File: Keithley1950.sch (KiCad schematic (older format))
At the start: 81 parts, among them J1 Conn_01x14, J2 Conn_01x03, J3 Conn_01x02, K1 Relay_SP2P, K2 Relay_SP2P, K3 Relay_SP3P, K4 Relay_SP2P, K5 Relay_SP2P, K6 Relay_SP3P, K7 Relay_SP3P, Q1 MMBFJ111, Q2 MMBFJ111, Q3 MMBFJ111, Q4 MMBFJ111, Q5 MMBT3906, Q6 MMBT3906, Q7 MMBFJ111, Q8 MMBT3906, U1 TL082, U2 LM339, U3 74LS138, U4 AD8436, U5 ULN2003, U6 74HC4094, U7 TL082

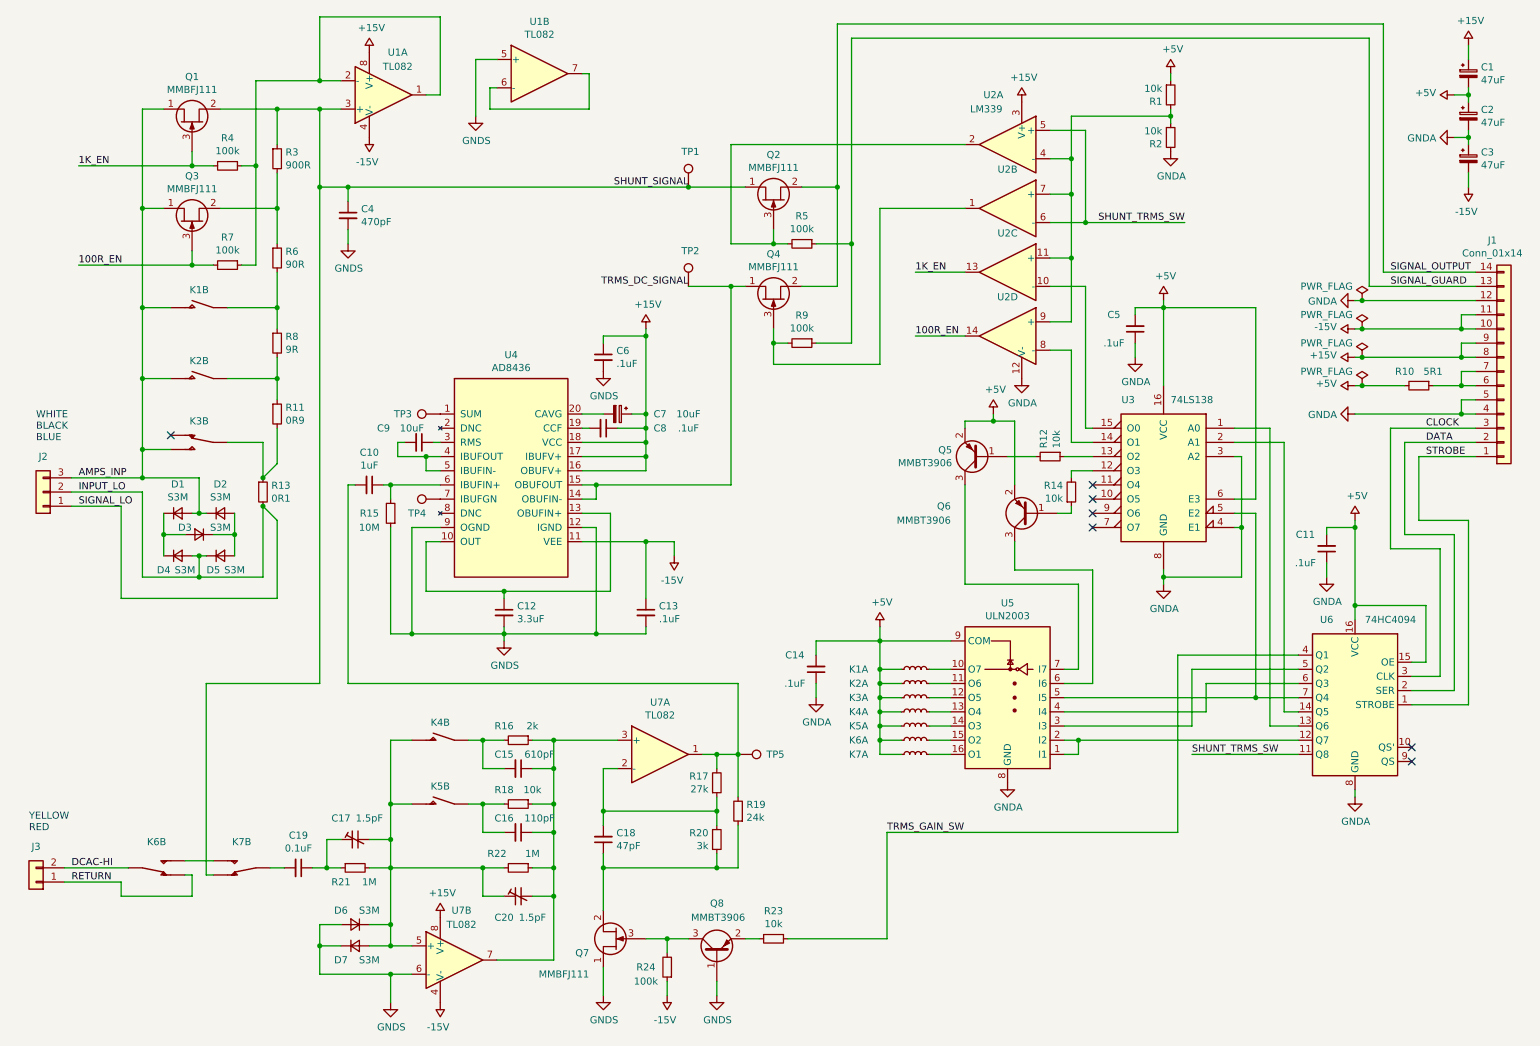
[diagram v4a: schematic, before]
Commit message: Switch to 2 serial resistors for shunts in schematic
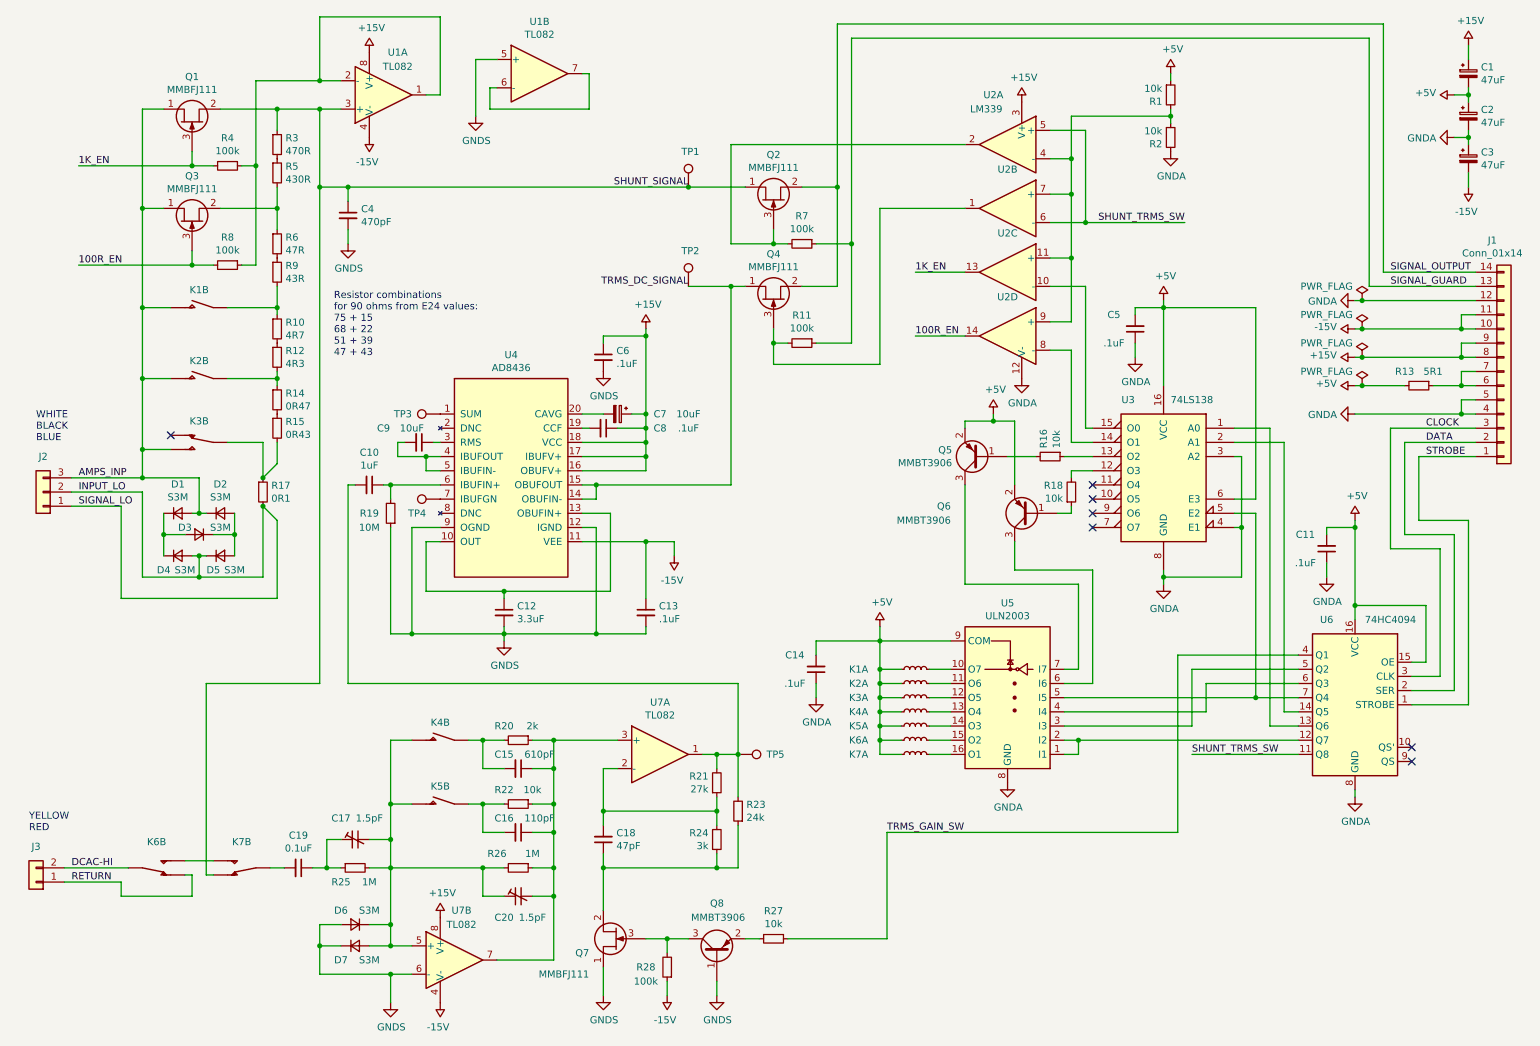
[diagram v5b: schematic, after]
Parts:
- added R10: 4R7, Resistor_SMD:R_0805_2012Metric, symbol Device:R_Small
- added R14: 0R47, Resistor_SMD:R_2512_6332Metric, symbol Device:R_Small
- added R3: 470R, Resistor_SMD:R_0805_2012Metric, symbol Device:R_Small
- added R6: 47R, Resistor_SMD:R_0805_2012Metric, symbol Device:R_Small
- R12: renamed from R8; value 9R -> 4R3
- R15: renamed from R11; value 0R9 -> 0R43; footprint project:R_2512_x2_serial -> Resistor_SMD:R_2512_6332Metric
- R5: renamed from R3; value 900R -> 430R; footprint project:R_0805_x2_Serial -> Resistor_SMD:R_0805_2012Metric
- R9: renamed from R6; value 90R -> 43R; footprint project:R_0805_x2_Serial -> Resistor_SMD:R_0805_2012Metric
- renumbered R9 to R11, R10 to R13, R12 to R16, R13 to R17, R14 to R18, R15 to R19, R16 to R20, R17 to R21, R18 to R22, R19 to R23, R20 to R24, R21 to R25, R22 to R26, R23 to R27, R24 to R28, R5 to R7, R7 to R8
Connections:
- net SHUNT_SIGNAL: now also R3.1; no longer R5.1
- net at Q3.2 (S), R5.2: now also R6.1; no longer R9.1
- net at K2.1, R12.2: now also R14.1; no longer R15.1
- net at K1.1, R9.2: now also R10.1; no longer R12.1
- new net: R6.2, R9.1
- new net: R10.2, R12.1
- new net: R14.2, R15.1
- new net: R3.2, R5.1
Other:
- note added: "Resistor combinations\nfor 90 ohms from E24 values:\n75 + 15\n68 + 22\n51 + 39\n47 + 43"
- moved on the sheet: R12, R15, R5, R9
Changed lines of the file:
@@
 $EndComp
 $Comp
-L Device:R_Small R6
+L Device:R_Small R9
 U 1 1 5CB9B972
-P 2350 2250
-F 0 "R6" H 2409 2296 50  0000 L CNN
-F 1 "90R" H 2409 2205 50  0000 L CNN
-F 2 "project:R_0805_x2_Serial" H 2350 2250 50  0001 C CNN
-F 3 "~" H 2350 2250 50  0001 C CNN
-F 4 "0.1%" H 2350 2250 50  0001 C CNN "Comment"
-	1    2350 2250
-	1    0    0    -1
-$EndComp
-$Comp
-L Device:R_Small R8
+P 2350 2350
+F 0 "R9" H 2409 2396 50  0000 L CNN
+F 1 "43R" H 2409 2305 50  0000 L CNN
+F 2 "Resistor_SMD:R_0805_2012Metric" H 2350 2350 50  0001 C CNN
+F 3 "~" H 2350 2350 50  0001 C CNN
+F 4 "0.1%" H 2350 2350 50  0001 C CNN "Comment"
+	1    2350 2350
+	1    0    0    -1
+$EndComp
+$Comp
+L Device:R_Small R12
 U 1 1 5CB9C495
-P 2350 2850
-F 0 "R8" H 2409 2896 50  0000 L CNN
-F 1 "9R" H 2409 2805 50  0000 L CNN
-F 2 "Resistor_SMD:R_0805_2012Metric" H 2350 2850 50  0001 C CNN
-F 3 "~" H 2350 2850 50  0001 C CNN
-F 4 "0.1%" H 2350 2850 50  0001 C CNN "Comment"
-	1    2350 2850
-	1    0    0    -1
-$EndComp
-$Comp
-L Device:R_Small R11
+P 2350 2950
+F 0 "R12" H 2409 2996 50  0000 L CNN
+F 1 "4R3" H 2409 2905 50  0000 L CNN
+F 2 "Resistor_SMD:R_0805_2012Metric" H 2350 2950 50  0001 C CNN
+F 3 "~" H 2350 2950 50  0001 C CNN
+F 4 "0.1%" H 2350 2950 50  0001 C CNN "Comment"
+	1    2350 2950
+	1    0    0    -1
+$EndComp
+$Comp
+L Device:R_Small R15
 U 1 1 5CB9C79B
-P 2350 3350
-F 0 "R11" H 2409 3396 50  0000 L CNN
-F 1 "0R9" H 2409 3305 50  0000 L CNN
-F 2 "project:R_2512_x2_serial" H 2350 3350 50  0001 C CNN
-F 3 "~" H 2350 3350 50  0001 C CNN
-F 4 "0.1%" H 2350 3350 50  0001 C CNN "Comment"
-	1    2350 3350
-	1    0    0    -1
-$EndComp
-$Comp
-L Device:R_Small R13
+P 2350 3450
+F 0 "R15" H 2409 3496 50  0000 L CNN
+F 1 "0R43" H 2409 3405 50  0000 L CNN
+F 2 "Resistor_SMD:R_2512_6332Metric" H 2350 3450 50  0001 C CNN
+F 3 "~" H 2350 3450 50  0001 C CNN
+F 4 "0.1%" H 2350 3450 50  0001 C CNN "Comment"
+	1    2350 3450
+	1    0    0    -1
+$EndComp
+$Comp
+L Device:R_Small R17
 U 1 1 5CB9CB8C
 P 2250 3900
-F 0 "R13" H 2309 3946 50  0000 L CNN
+F 0 "R17" H 2309 3946 50  0000 L CNN
 F 1 "0R1" H 2309 3855 50  0000 L CNN
 F 2 "project:R_2512_With_10mm_axial" H 2250 3900 50  0001 C CNN
@@
 $EndComp
 $Comp
-L Device:R_Small R3
+L Device:R_Small R5
 U 1 1 5CB9CE54
-P 2350 1550
-F 0 "R3" H 2409 1596 50  0000 L CNN
-F 1 "900R" H 2409 1505 50  0000 L CNN
-F 2 "project:R_0805_x2_Serial" H 2350 1550 50  0001 C CNN
-F 3 "~" H 2350 1550 50  0001 C CNN
-F 4 "0.1%" H 2350 1550 50  0001 C CNN "Comment"
-	1    2350 1550
+P 2350 1650
+F 0 "R5" H 2409 1696 50  0000 L CNN
+F 1 "430R" H 2409 1605 50  0000 L CNN
+F 2 "Resistor_SMD:R_0805_2012Metric" H 2350 1650 50  0001 C CNN
+F 3 "~" H 2350 1650 50  0001 C CNN
+F 4 "0.1%" H 2350 1650 50  0001 C CNN "Comment"
+	1    2350 1650
 	1    0    0    -1
 $EndComp
@@
 $EndComp
 $Comp
-L Device:R_Small R7
+L Device:R_Small R8
 U 1 1 5CB9E6FE
 P 2000 2300
-F 0 "R7" V 1804 2300 50  0000 C CNN
+F 0 "R8" V 1804 2300 50  0000 C CNN
 F 1 "100k" V 1895 2300 50  0000 C CNN
 F 2 "Resistor_SMD:R_0805_2012Metric" H 2000 2300 50  0001 C CNN
@@
 $EndComp
 $Comp
-L Device:R_Small R5
+L Device:R_Small R7
 U 1 1 5CB9EC31
 P 6050 2150
-F 0 "R5" V 5854 2150 50  0000 C CNN
+F 0 "R7" V 5854 2150 50  0000 C CNN
 F 1 "100k" V 5945 2150 50  0000 C CNN
 F 2 "Resistor_SMD:R_0805_2012Metric" H 6050 2150 50  0001 C CNN
@@
 $EndComp
 $Comp
-L Device:R_Small R9
+L Device:R_Small R11
 U 1 1 5CB9F858
 P 6050 2850
-F 0 "R9" V 5854 2850 50  0000 C CNN
+F 0 "R11" V 5854 2850 50  0000 C CNN
 F 1 "100k" V 5945 2850 50  0000 C CNN
 F 2 "Resistor_SMD:R_0805_2012Metric" H 6050 2850 50  0001 C CNN
@@
 $EndComp
 $Comp
-L Device:R_Small R21
+L Device:R_Small R25
 U 1 1 5CB9FCE1
 P 2900 6550
-F 0 "R21" V 3000 6650 50  0000 C CNN
+F 0 "R25" V 3000 6650 50  0000 C CNN
 F 1 "1M" V 3000 6450 50  0000 C CNN
 F 2 "Resistor_SMD:R_0805_2012Metric" H 2900 6550 50  0001 C CNN
@@
 $EndComp
 $Comp
-L Device:R_Small R22
+L Device:R_Small R26
 U 1 1 5CBA1211
 P 4050 6550
-F 0 "R22" V 3950 6400 50  0000 C CNN
+F 0 "R26" V 3950 6400 50  0000 C CNN
 F 1 "1M" V 3950 6650 50  0000 C CNN
 F 2 "Resistor_SMD:R_0805_2012Metric" H 4050 6550 50  0001 C CNN
@@
 $EndComp
 $Comp
-L Device:R_Small R18
+L Device:R_Small R22
 U 1 1 5CBA173C
 P 4050 6100
-F 0 "R18" V 3950 6000 50  0000 C CNN
+F 0 "R22" V 3950 6000 50  0000 C CNN
 F 1 "10k" V 3950 6200 50  0000 C CNN
 F 2 "Resistor_SMD:R_0805_2012Metric" H 4050 6100 50  0001 C CNN
@@
 $EndComp
 $Comp
-L Device:R_Small R16
+L Device:R_Small R20
 U 1 1 5CBA2121
 P 4050 5650
-F 0 "R16" V 3950 5550 50  0000 C CNN
+F 0 "R20" V 3950 5550 50  0000 C CNN
 F 1 "2k" V 3950 5750 50  0000 C CNN
 F 2 "Resistor_SMD:R_0805_2012Metric" H 4050 5650 50  0001 C CNN
@@
 $EndComp
 $Comp
-L Device:R_Small R17
+L Device:R_Small R21
 U 1 1 5CBA2530
 P 5450 5950
-F 0 "R17" H 5391 5904 50  0000 R CNN
+F 0 "R21" H 5391 5904 50  0000 R CNN
 F 1 "27k" H 5391 5995 50  0000 R CNN
 F 2 "Resistor_SMD:R_0805_2012Metric" H 5450 5950 50  0001 C CNN
@@
 $EndComp
 $Comp
-L Device:R_Small R19
+L Device:R_Small R23
 U 1 1 5CBA3019
 P 5600 6150
-F 0 "R19" H 5541 6104 50  0000 R CNN
+F 0 "R23" H 5541 6104 50  0000 R CNN
 F 1 "24k" H 5541 6195 50  0000 R CNN
 F 2 "Resistor_SMD:R_0805_2012Metric" H 5600 6150 50  0001 C CNN
@@
 $EndComp
 $Comp
-L Device:R_Small R24
+L Device:R_Small R28
 U 1 1 5CBA7132
 P 5100 7250
-F 0 "R24" H 5250 7250 50  0000 C CNN
+F 0 "R28" H 5250 7250 50  0000 C CNN
 F 1 "100k" H 5250 7350 50  0000 C CNN
 F 2 "Resistor_SMD:R_0805_2012Metric" H 5100 7250 50  0001 C CNN
@@
 	2000 2600 2350 2600
 Wire Wire Line
-	2350 2600 2350 2350
-Wire Wire Line
-	2350 2600 2350 2750
-Connection ~ 2350 2600
-Wire Wire Line
-	2350 2950 2350 3100
+	2350 2600 2350 2450
+Wire Wire Line
+	2350 3050 2350 3100
 Wire Wire Line
 	1600 3600 1400 3600
@@
 	2250 3800 2350 3700
 Wire Wire Line
-	2350 3700 2350 3450
+	2350 3700 2350 3550
 Wire Wire Line
 	2250 3550 2000 3550
@@
 $EndComp
 Wire Wire Line
-	2350 2150 2350 1900
-Wire Wire Line
-	1950 1200 2350 1200
-Wire Wire Line
-	2350 1200 2350 1450
-Wire Wire Line
-	2350 1200 2650 1200
-Connection ~ 2350 1200
-Wire Wire Line
 	2650 1200 2650 1750
 Wire Wire Line
@@
 Wire Wire Line
 	1950 1900 2350 1900
-Connection ~ 2350 1900
-Wire Wire Line
-	2350 1900 2350 1650
+Wire Wire Line
+	2350 1900 2350 1750
 Wire Wire Line
 	1750 2200 1750 2300
@@
 Wire Wire Line
 	2000 3100 2350 3100
-Connection ~ 2350 3100
-Wire Wire Line
-	2350 3100 2350 3250
 Wire Wire Line
 	10800 2350 10150 2350
@@
 $EndComp
 $Comp
-L Device:R_Small R10
+L Device:R_Small R13
 U 1 1 5D058670
 P 10400 3150
-F 0 "R10" V 10300 3050 50  0000 C CNN
+F 0 "R13" V 10300 3050 50  0000 C CNN
 F 1 "5R1" V 10300 3250 50  0000 C CNN
 F 2 "Resistor_SMD:R_2512_6332Metric" H 10400 3150 50  0001 C CNN
@@
 $EndComp
 $Comp
-L Device:R_Small R12
+L Device:R_Small R16
 U 1 1 5D0A1B8F
 P 7800 3650
-F 0 "R12" H 7741 3604 50  0000 R CNN
+F 0 "R16" H 7741 3604 50  0000 R CNN
 F 1 "10k" H 7741 3695 50  0000 R CNN
 F 2 "Resistor_SMD:R_0805_2012Metric" H 7800 3650 50  0001 C CNN
@@
 $EndComp
 $Comp
-L Device:R_Small R14
+L Device:R_Small R18
 U 1 1 5D0A23C6
 P 7950 3900
-F 0 "R14" H 7891 3854 50  0000 R CNN
+F 0 "R18" H 7891 3854 50  0000 R CNN
 F 1 "10k" H 7891 3945 50  0000 R CNN
 F 2 "Resistor_SMD:R_0805_2012Metric" H 7950 3900 50  0001 C CNN
@@
 	9550 5050 8700 5050
 $Comp
-L Device:R_Small R23
+L Device:R_Small R27
 U 1 1 5D34A213
 P 5850 7050
-F 0 "R23" V 5654 7050 50  0000 C CNN
+F 0 "R27" V 5654 7050 50  0000 C CNN
 F 1 "10k" V 5745 7050 50  0000 C CNN
 F 2 "Resistor_SMD:R_0805_2012Metric" H 5850 7050 50  0001 C CNN
@@
 $EndComp
 $Comp
-L Device:R_Small R20
+L Device:R_Small R24
 U 1 1 5CBA2B42
 P 5450 6350
-F 0 "R20" H 5391 6304 50  0000 R CNN
+F 0 "R24" H 5391 6304 50  0000 R CNN
 F 1 "3k" H 5391 6395 50  0000 R CNN
 F 2 "Resistor_SMD:R_0805_2012Metric" H 5450 6350 50  0001 C CNN
@@
 $EndComp
 $Comp
-L Device:R_Small R15
+L Device:R_Small R19
 U 1 1 5DE4A83A
 P 3150 4050
-F 0 "R15" H 3300 4050 50  0000 C CNN
+F 0 "R19" H 3300 4050 50  0000 C CNN
 F 1 "10M" H 3300 4150 50  0000 C CNN
 F 2 "Resistor_SMD:R_0805_2012Metric" H 3150 4050 50  0001 C CNN
@@
 Wire Wire Line
 	3950 4850 3950 4900
+$Comp
+L Device:R_Small R14
+U 1 1 5CF7C450
+P 2350 3250
+F 0 "R14" H 2409 3296 50  0000 L CNN
+F 1 "0R47" H 2409 3205 50  0000 L CNN
+F 2 "Resistor_SMD:R_2512_6332Metric" H 2350 3250 50  0001 C CNN
+F 3 "~" H 2350 3250 50  0001 C CNN
+F 4 "0.1%" H 2350 3250 50  0001 C CNN "Comment"
+	1    2350 3250
+	1    0    0    -1
+$EndComp
+Wire Wire Line
+	2350 3150 2350 3100
+Connection ~ 2350 3100
+$Comp
+L Device:R_Small R10
+U 1 1 5CFD46A4
+P 2350 2750
+F 0 "R10" H 2409 2796 50  0000 L CNN
+F 1 "4R7" H 2409 2705 50  0000 L CNN
+F 2 "Resistor_SMD:R_0805_2012Metric" H 2350 2750 50  0001 C CNN
+F 3 "~" H 2350 2750 50  0001 C CNN
+F 4 "0.1%" H 2350 2750 50  0001 C CNN "Comment"
+	1    2350 2750
+	1    0    0    -1
+$EndComp
+Wire Wire Line
+	2350 2650 2350 2600
+Connection ~ 2350 2600
+$Comp
+L Device:R_Small R6
+U 1 1 5D02CDB2
+P 2350 2150
+F 0 "R6" H 2409 2196 50  0000 L CNN
+F 1 "47R" H 2409 2105 50  0000 L CNN
+F 2 "Resistor_SMD:R_0805_2012Metric" H 2350 2150 50  0001 C CNN
+F 3 "~" H 2350 2150 50  0001 C CNN
+F 4 "0.1%" H 2350 2150 50  0001 C CNN "Comment"
+	1    2350 2150
+	1    0    0    -1
+$EndComp
+Wire Wire Line
+	2350 2050 2350 1900
+Connection ~ 2350 1900
+Wire Wire Line
+	1950 1200 2350 1200
+$Comp
+L Device:R_Small R3
+U 1 1 5D0856A1
+P 2350 1450
+F 0 "R3" H 2409 1496 50  0000 L CNN
+F 1 "470R" H 2409 1405 50  0000 L CNN
+F 2 "Resistor_SMD:R_0805_2012Metric" H 2350 1450 50  0001 C CNN
+F 3 "~" H 2350 1450 50  0001 C CNN
+F 4 "0.1%" H 2350 1450 50  0001 C CNN "Comment"
+	1    2350 1450
+	1    0    0    -1
+$EndComp
+Wire Wire Line
+	2350 1350 2350 1200
+Connection ~ 2350 1200
+Wire Wire Line
+	2350 1200 2650 1200
+Text Notes 2750 2950 0    50   ~ 0
+Resistor combinations\nfor 90 ohms from E24 values:\n75 + 15\n68 + 22\n51 + 39\n47 + 43
 $EndSCHEMATC

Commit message: Add TZ03 model, some tweaks
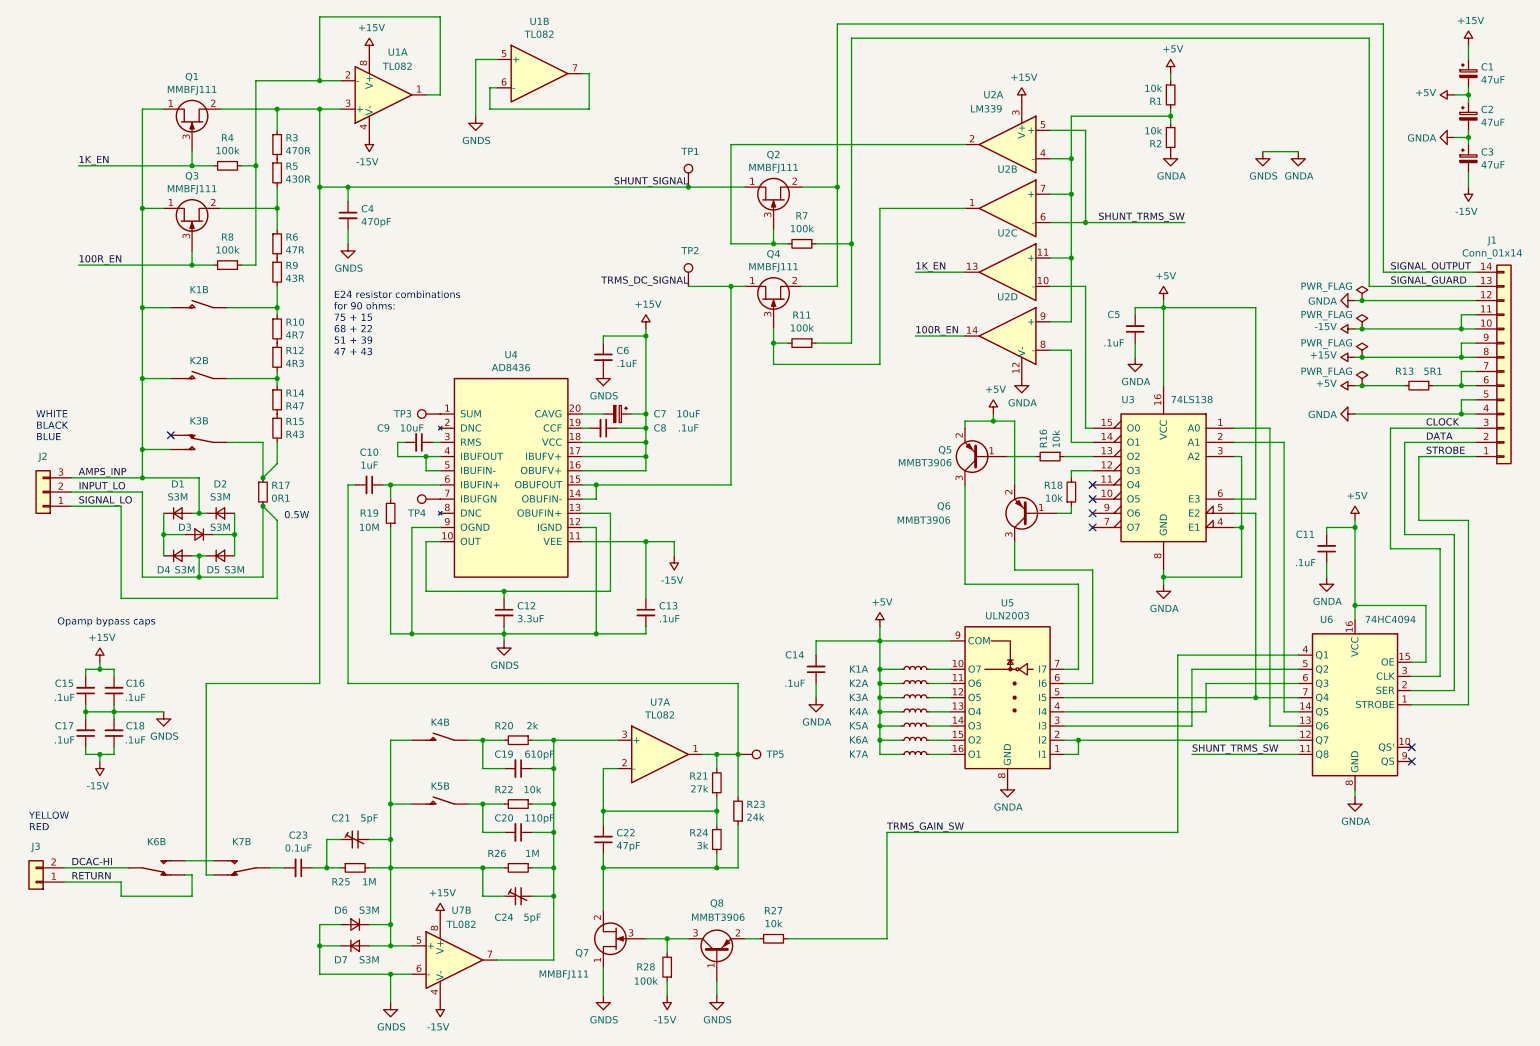
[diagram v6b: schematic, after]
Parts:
- added C15, C16, C17, C18: .1uF, Capacitor_SMD:C_0603_1608Metric, symbol Device:C_Small
- C21: renamed from C17; value 1.5pF -> 5pF; footprint Capacitor_SMD:C_Trimmer_Murata_TZB4-B -> project:MURATA_TZ03
- C24: renamed from C20; value 1.5pF -> 5pF; footprint Capacitor_SMD:C_Trimmer_Murata_TZB4-B -> project:MURATA_TZ03
- R14: value 0R47 -> R47
- R15: value 0R43 -> R43
- renumbered C15 to C19, C16 to C20, C18 to C22, C19 to C23
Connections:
- net GNDS is gone; now on net GNDA: C12.2, C13.2, C4.2, C6.2, D6.2 (A), D7.1 (K), Q7.1 (D), Q8.1 (B), R19.1, U1.5 (+), U4.12 (IGND), U4.9 (OGND), U7.6 (-)
- net +15V: now also C15.2, C16.2
- net -15V: now also C17.1, C18.1
- net GNDA: now also C15.1, C16.1, C17.2, C18.2
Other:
- note added: "0.5W"
- note added: "E24 resistor combinations\nfor 90 ohms:\n75 + 15\n68 + 22\n51 + 39\n47 + 43"
- note added: "Opamp bypass caps"
- note removed: "Resistor combinations\nfor 90 ohms from E24 values:\n75 + 15\n68 + 22\n51 + 39\n47 + 43"
